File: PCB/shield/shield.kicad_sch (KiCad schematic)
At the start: 13 parts, among them J1 QTR-8A, J10 ESP32_left_m, J11 ESP32_right_m, J12 Barrel_Jack, J2 QMC5883L, J3 Servo, J4 LM2596S_in(+), J5 LM2596S_in(-), J6 LM2596S_out(+), J7 LM2596S_out(-)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

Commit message: wip: pcb tracks
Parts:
- added J13: Conn_01x06, Connector_JST:JST_XH_B6B-XH-A_1x06_P2.50mm_Vertical, symbol Connector_Generic:Conn_01x06
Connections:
- net +3V3: now also J13.5 (Pin_5)
- net GND: now also J13.2 (Pin_2)
- net GPIO13: now also J13.3 (Pin_3)
- net GPIO14: now also J13.4 (Pin_4)
- net GPIO17: now also J13.1 (Pin_1)
- net GPIO18: now also J13.6 (Pin_6)

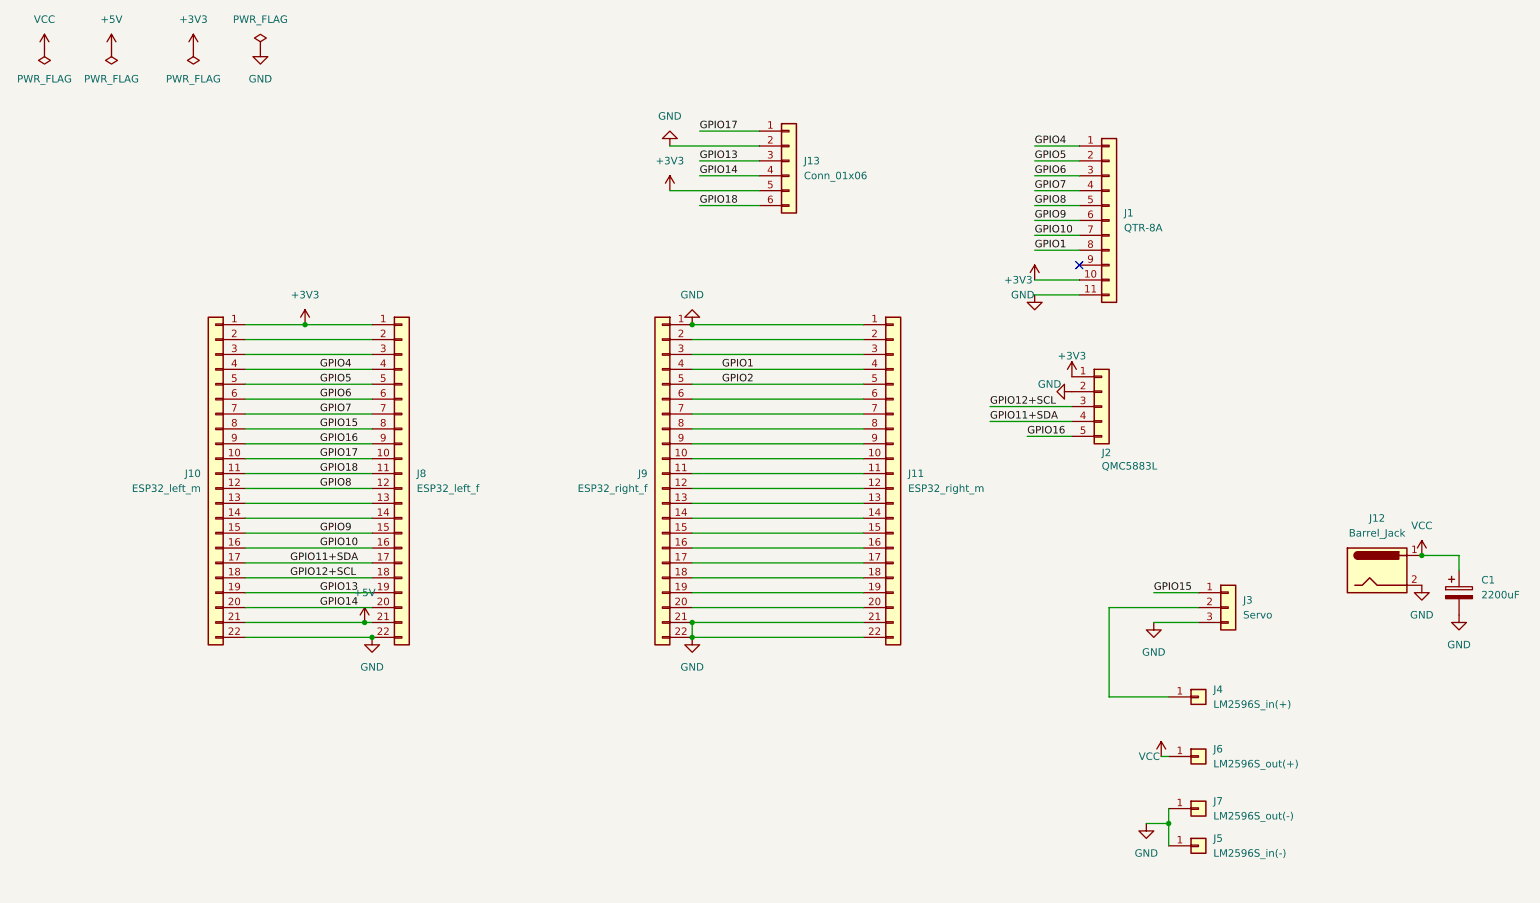
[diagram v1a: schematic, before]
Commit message: wip: adding tracks on pcb, adding 7805 regulator
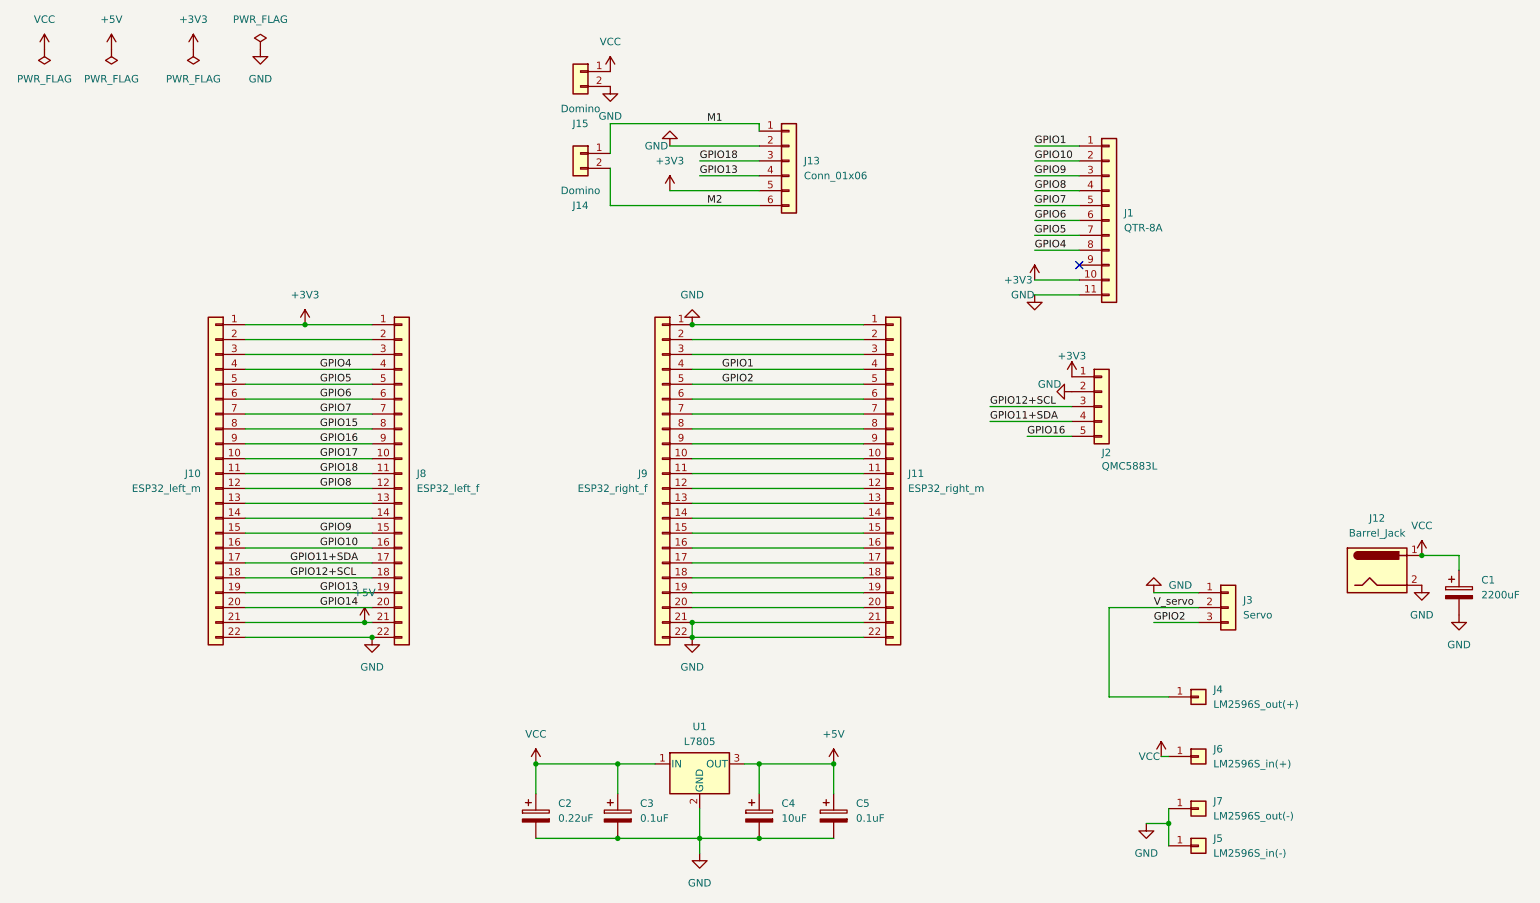
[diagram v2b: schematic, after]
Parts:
- added C2: 0.22uF, Capacitor_THT:CP_Radial_D5.0mm_P2.00mm, symbol Device:C_Polarized
- added C3, C5: 0.1uF, Capacitor_THT:CP_Radial_Tantal_D4.5mm_P2.50mm, symbol Device:C_Polarized
- added C4: 10uF, Capacitor_THT:CP_Radial_D5.0mm_P2.00mm, symbol Device:C_Polarized
- added J14, J15: Domino, TerminalBlock_Phoenix:TerminalBlock_Phoenix_MKDS-1,5-2_1x02_P5.00mm_Horizontal, symbol Connector_Generic:Conn_01x02
- added U1: L7805, Package_TO_SOT_THT:TO-220-3_Horizontal_TabDown, symbol Regulator_Linear:L7805
- J4: value LM2596S_in(+) -> LM2596S_out(+)
- J6: value LM2596S_out(+) -> LM2596S_in(+)
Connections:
- net +5V: now also C4.1, C5.1, U1.3 (OUT)
- net GND: now also J3.1 (Pin_1), C2.2, C3.2, C4.2, C5.2, J15.2 (Pin_2), U1.2 (GND); no longer J3.3 (Pin_3)
- net GPIO1: now also J1.1 (Pin_1); no longer J1.8 (Pin_8)
- net GPIO10: now also J1.2 (Pin_2); no longer J1.7 (Pin_7)
- net GPIO13: now also J13.4 (Pin_4); no longer J13.3 (Pin_3)
- net GPIO14: no longer J13.4 (Pin_4)
- net GPIO15: no longer J3.1 (Pin_1)
- net GPIO17: no longer J13.1 (Pin_1)
- net GPIO18: now also J13.3 (Pin_3); no longer J13.6 (Pin_6)
- net GPIO2: now also J3.3 (Pin_3)
- net GPIO4: now also J1.8 (Pin_8); no longer J1.1 (Pin_1)
- net GPIO5: now also J1.7 (Pin_7); no longer J1.2 (Pin_2)
- net GPIO6: now also J1.6 (Pin_6); no longer J1.3 (Pin_3)
- net GPIO7: now also J1.5 (Pin_5); no longer J1.4 (Pin_4)
- net GPIO8: now also J1.4 (Pin_4); no longer J1.5 (Pin_5)
- net GPIO9: now also J1.3 (Pin_3); no longer J1.6 (Pin_6)
- net VCC: now also C2.1, C3.1, J15.1 (Pin_1), U1.1 (IN)
- net V_servo: now reaches J3.2 (Pin_2), J4.1 (Pin_1)
- new net M1: J13.1 (Pin_1), J14.1 (Pin_1)
- new net M2: J13.6 (Pin_6), J14.2 (Pin_2)

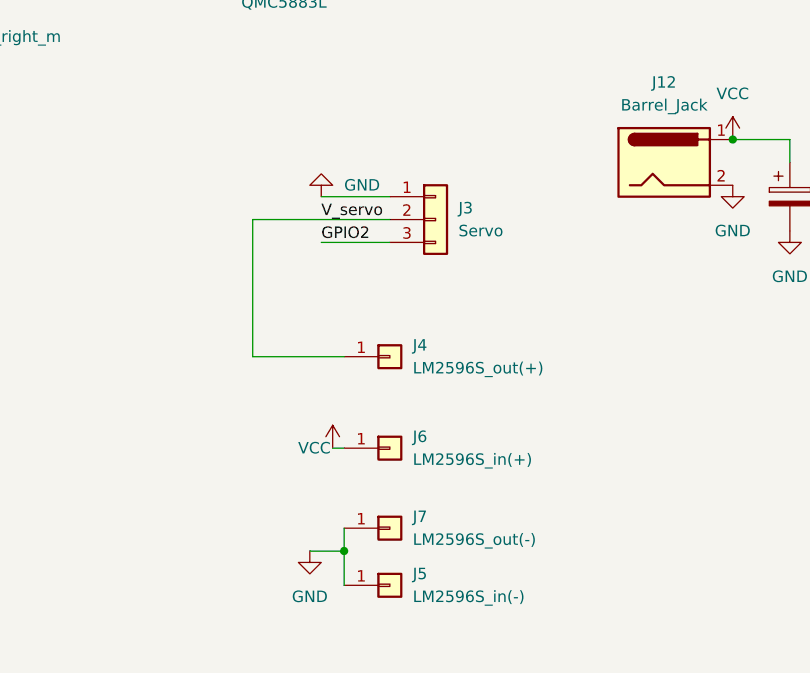
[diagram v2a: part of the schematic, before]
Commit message: feat: added pcb traces and remove lm2596s
Added all required pcb traces.
Remove LM2596S footprint
Added LM7805 5V regulator
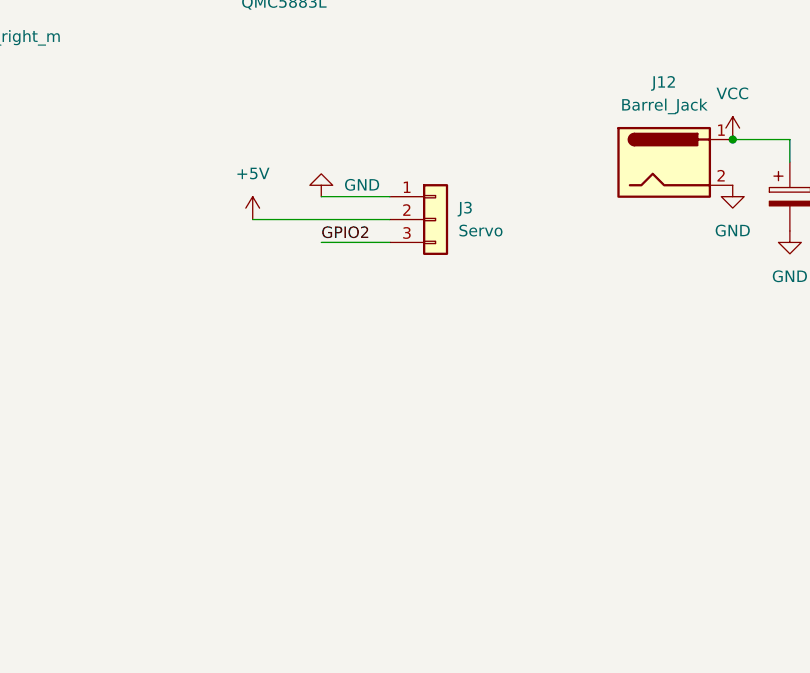
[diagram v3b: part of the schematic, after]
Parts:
- removed J4: LM2596S_out(+), Connector_PinSocket_2.54mm:PinSocket_1x01_P2.54mm_Vertical, symbol Connector_Generic:Conn_01x01
- removed J5: LM2596S_in(-), Connector_PinSocket_2.54mm:PinSocket_1x01_P2.54mm_Vertical, symbol Connector_Generic:Conn_01x01
- removed J6: LM2596S_in(+), Connector_PinSocket_2.54mm:PinSocket_1x01_P2.54mm_Vertical, symbol Connector_Generic:Conn_01x01
- removed J7: LM2596S_out(-), Connector_PinSocket_2.54mm:PinSocket_1x01_P2.54mm_Vertical, symbol Connector_Generic:Conn_01x01
- U1: footprint Package_TO_SOT_THT:TO-220-3_Horizontal_TabDown -> Package_TO_SOT_THT:TO-220-3_Vertical
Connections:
- net V_servo is gone; now on net +5V: J3.2 (Pin_2)

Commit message: feat: added a  button
Updated button switch THT library
Added a button connected to GPIO15
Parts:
- added SW1: SW_Push, Button_Switch_THT:SW_PUSH_6mm_H5mm, symbol Switch:SW_Push
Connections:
- net +3V3: now also SW1.1
- net GPIO15: now also SW1.2
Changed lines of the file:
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@@
 		)
 	)
+	(label "GPIO15"
+		(at 72.39 148.59 0)
+		(effects
+			(font
+				(size 1.27 1.27)
+			)
+			(justify left bottom)
+		)
+	)
 	(label "GPIO8"
 		(at 73.66 100.33 0)
@@
 	)
 	(symbol
+		(lib_id "Switch:SW_Push")
+		(at 67.31 148.59 0)
+		(unit 1)
+		(exclude_from_sim no)
+		(in_bom yes)
+		(on_board yes)
+		(dnp no)
+		(fields_autoplaced yes)
+		(property "Reference" "SW1"
+			(at 67.31 140.97 0)
+			(effects
+				(font
+					(size 1.27 1.27)
+				)
+			)
+		)
+		(property "Value" "SW_Push"
+			(at 67.31 143.51 0)
+			(effects
+				(font
+					(size 1.27 1.27)
+				)
+			)
+		)
+		(property "Footprint" "Button_Switch_THT:SW_PUSH_6mm_H5mm"
+			(at 67.31 143.51 0)
+			(effects
+				(font
+					(size 1.27 1.27)
+				)
+				(hide yes)
+			)
+		)
+		(property "Datasheet" "~"
+			(at 67.31 143.51 0)
+			(effects
+				(font
+					(size 1.27 1.27)
+				)
+				(hide yes)
+			)
+		)
+		(property "Description" "Push button switch, generic, two pins"
+			(at 67.31 148.59 0)
+			(effects
+				(font
+					(size 1.27 1.27)
+				)
+				(hide yes)
+			)
+		)
+		(pin "2"
+		)
+		(pin "1"
+		)
+		(instances
+			(project ""
+				(path "/9a41b561-8e6b-4187-bd8f-1a6b5b887c54"
+					(reference "SW1")
+					(unit 1)
+				)
+			)
+		)
+	)
+	(symbol
 		(lib_id "Connector_Generic:Conn_01x22")
 		(at 132.08 97.79 0)
@@
 					(unit 1)
 				)
+			)
+		)
+	)
+	(symbol
+		(lib_id "power:+3V3")
+		(at 62.23 148.59 0)
+		(unit 1)
+		(exclude_from_sim no)
+		(in_bom yes)
+		(on_board yes)
+		(dnp no)
+		(property "Reference" "#PWR011"
+			(at 62.23 152.4 0)
+			(effects
+				(font
+					(size 1.27 1.27)
+				)
+				(hide yes)
+			)
+		)
+		(property "Value" "+3V3"
+			(at 59.436 148.59 0)
+			(effects
+				(font
+					(size 1.27 1.27)
+				)
+			)
+		)
+		(property "Footprint" ""
+			(at 62.23 148.59 0)
+			(effects
+				(font
+					(size 1.27 1.27)
+				)
+				(hide yes)
+			)
+		)
+		(property "Datasheet" ""
+			(at 62.23 148.59 0)
+			(effects
+				(font
+					(size 1.27 1.27)
+				)
+				(hide yes)
+			)
+		)
+		(property "Description" "Power symbol creates a global label with name \"+3V3\""
+			(at 62.23 148.59 0)
+			(effects
+				(font
+					(size 1.27 1.27)
+				)
+				(hide yes)
+			)
+		)
+		(pin "1"
+		)
+		(instances
+			(project ""
+				(path "/9a41b561-8e6b-4187-bd8f-1a6b5b887c54"
+					(reference "#PWR011")
+					(unit 1)
+				)

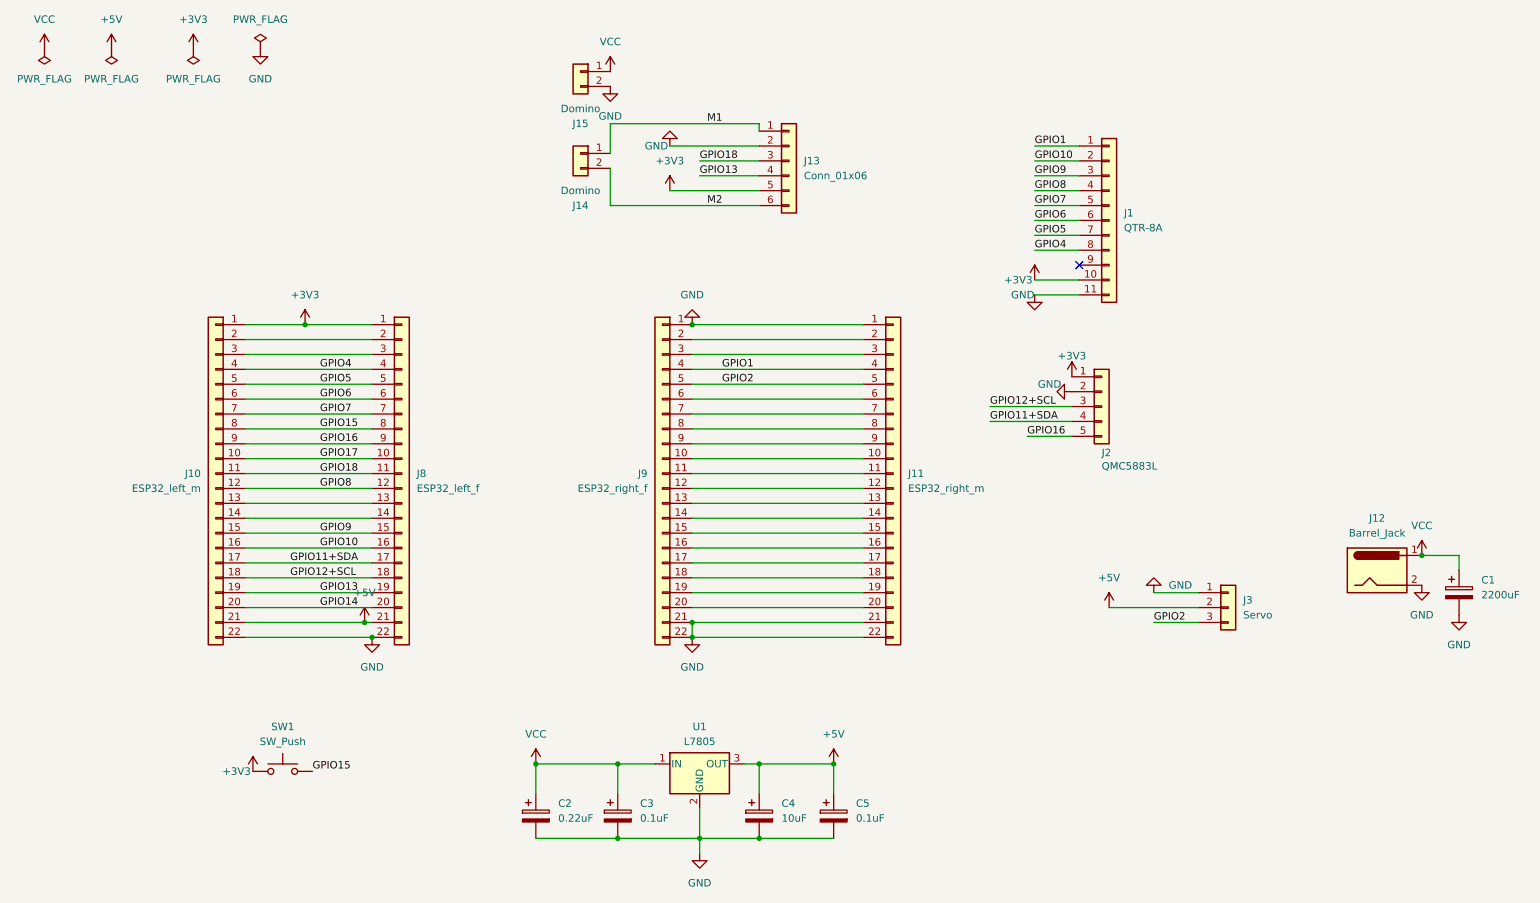
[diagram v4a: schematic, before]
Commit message: wip: adding reverse polar protection
Added 1N5822 to protect reverse polar
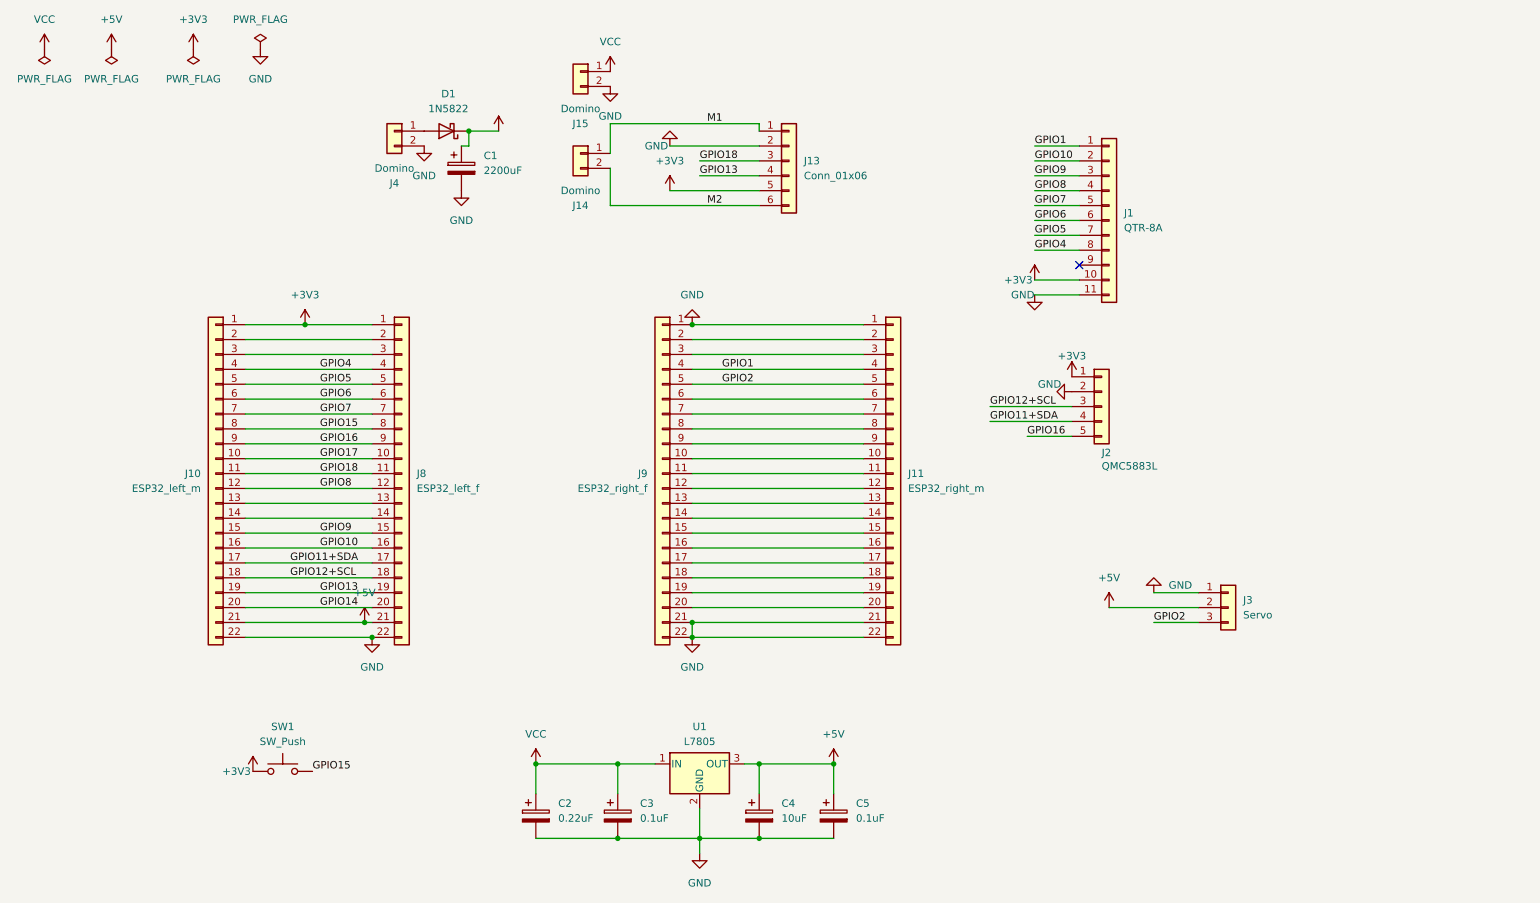
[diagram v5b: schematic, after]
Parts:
- removed J12: Barrel_Jack, Connector_BarrelJack:BarrelJack_GCT_DCJ200-10-A_Horizontal, symbol Connector:Barrel_Jack
- added D1: 1N5822, Diode_THT:D_DO-201AD_P15.24mm_Horizontal, symbol Diode:1N5822
- added J4: Domino, TerminalBlock_Phoenix:TerminalBlock_Phoenix_MKDS-1,5-2_1x02_P5.00mm_Horizontal, symbol Connector_Generic:Conn_01x02
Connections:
- net GND: now also J4.2 (Pin_2)
- net VCC: now also D1.1 (K)
- new net: D1.2 (A), J4.1 (Pin_1)
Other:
- moved on the sheet: C1
